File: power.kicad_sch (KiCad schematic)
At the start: 30 parts, among them J2 KYCO-P4S-S, J3 MicroFit_2x02, J3B1 DNI, J4 DC 24V/5A OUT, Q1 BC847, Q2 IRF9540SPBF, SW1 DNI, U1 MAX5035BUSA, U6 MC78M12BDTG

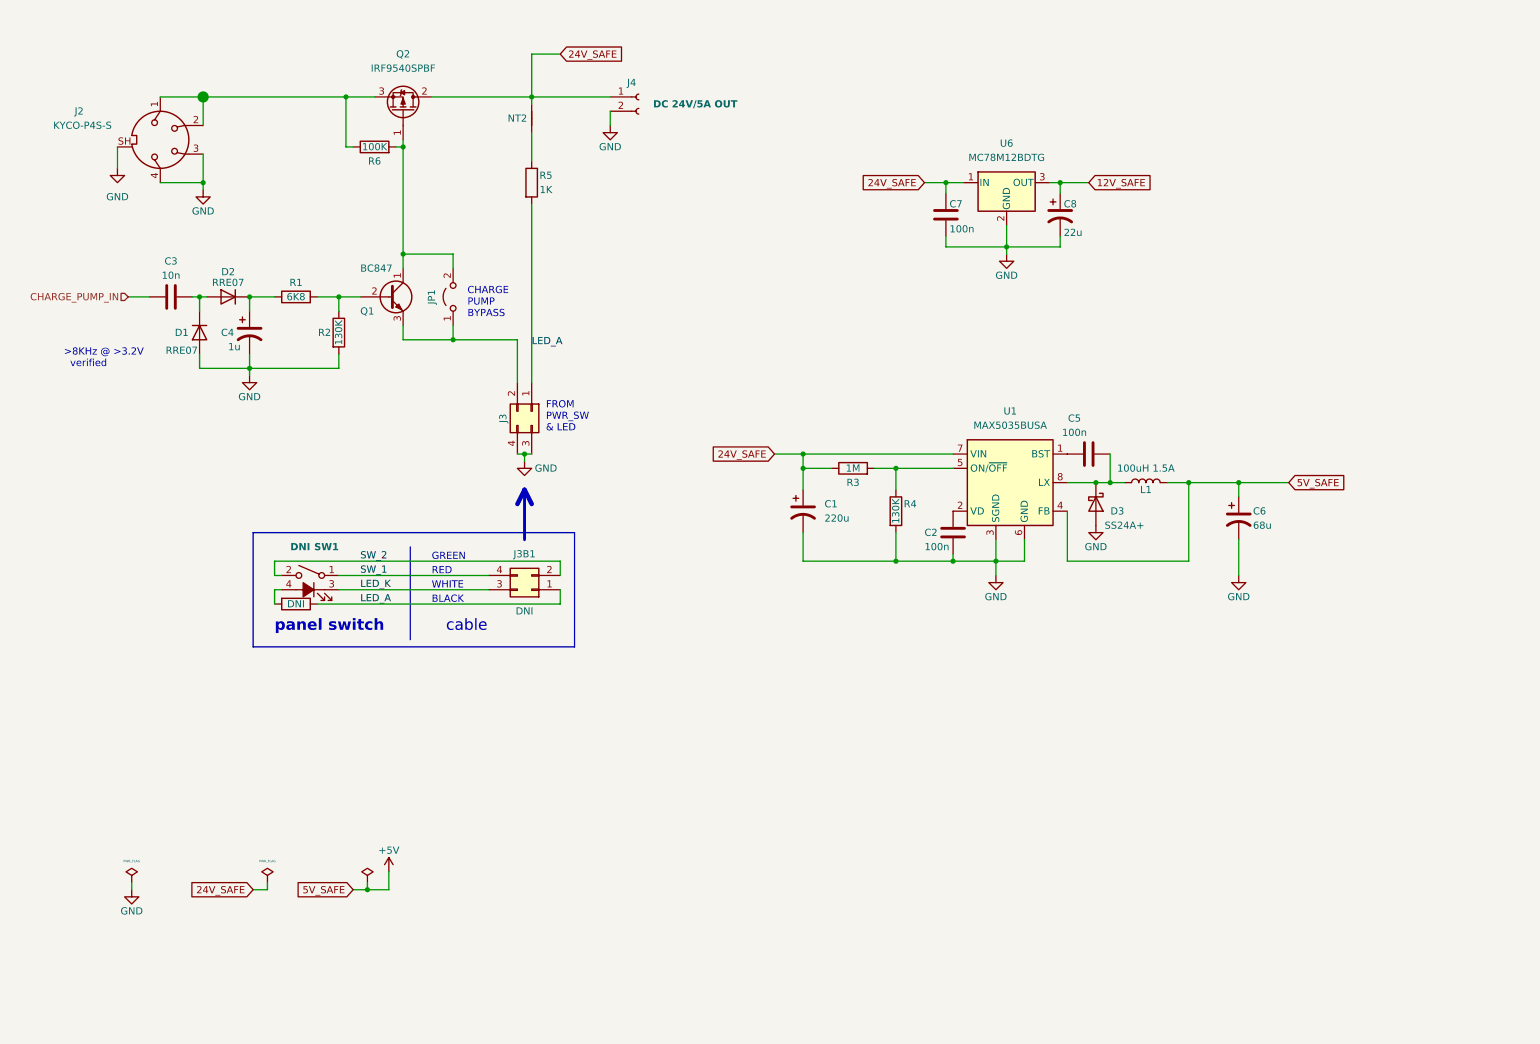
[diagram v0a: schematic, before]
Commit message: Reworked PSU control scheme (schematic only.)
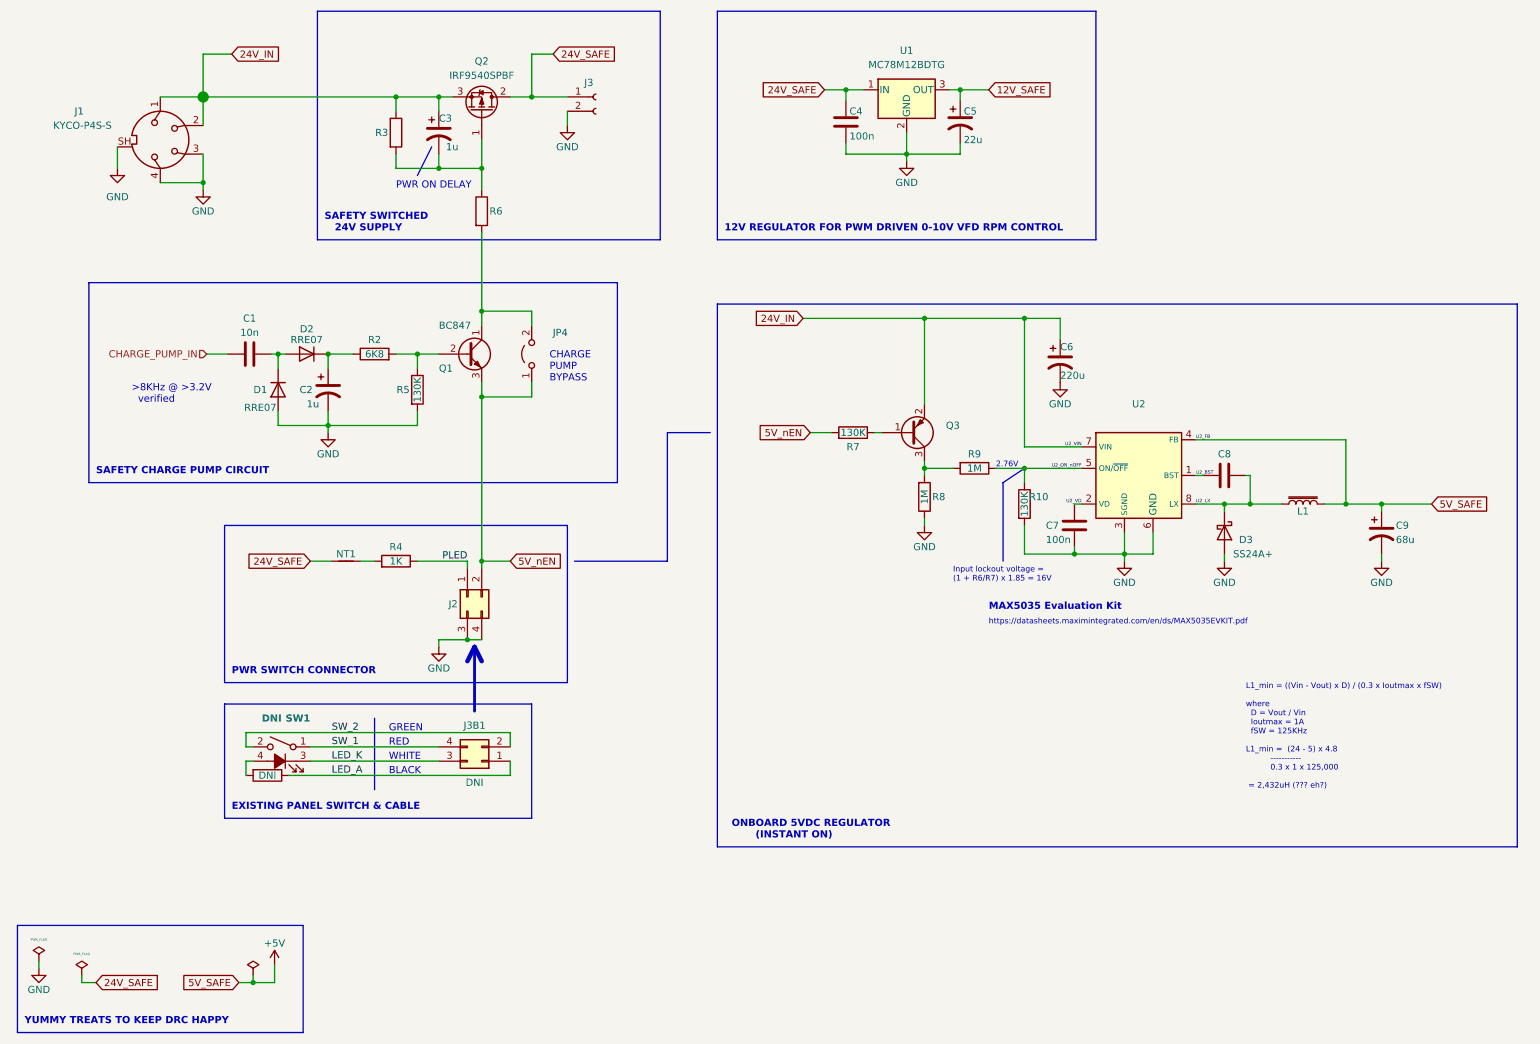
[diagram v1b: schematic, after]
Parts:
- added C3: 1u, Capacitor_SMD:C_0603_1608Metric, symbol Device:C_Polarized_US
- added Q3: (no value), Package_TO_SOT_SMD:SOT-23, symbol Transistor_BJT:BC857
- added R6: (no value), Resistor_SMD:R_0603_1608Metric, symbol Device:R
- added R7: 130K, Resistor_SMD:R_0603_1608Metric, symbol Device:R
- added R8: 1M, Resistor_SMD:R_0603_1608Metric, symbol Device:R
- C8: renamed from C5; value 100n -> (none)
- J3: renamed from J4; value DC 24V/5A OUT -> (none)
- L1: value 100uH 1.5A -> (none); footprint Inductor_SMD:L_12x12mm_H6mm -> (none); symbol Device:L -> 3rd-party:Lcore
- R3: renamed from R6; value 100K -> (none); footprint Resistor_SMD:R_0603_1608Metric -> (none)
- U2: renamed from U1; value MAX5035BUSA -> (none); footprint Package_SO:SOIC-8_3.9x4.9mm_P1.27mm -> (none); symbol Regulator_Switching:MAX5035BUSA -> 3rd-party:MAX5035BUSA
- renumbered C3 to C1, C4 to C2, C7 to C4, C8 to C5, C1 to C6, C2 to C7, C6 to C9, J2 to J1, J3 to J2, JP1 to JP4, NT2 to NT1, R101 to R1, R4 to R10, R1 to R2, R5 to R4, R2 to R5, R3 to R9, U6 to U1
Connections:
- net 24V_SAFE: no longer C6.1, R9.1, U2.7 (VIN)
- net GND: now also R8.1
- net LED_A: no longer J2.1 (Pin_1), R4.2
- net U2_LX: now reaches C8.2, D3.1 (K), L1.1, U2.8 (LX)
- net at JP4.2 (B), Q1.1 (C): now also R6.2; no longer Q2.1 (G), R3.2
- net 5V_nEN: now reaches J2.2 (Pin_2), JP4.1 (A), Q1.3 (E)
- net 5V_nEN: now also R7.2
- net U2_BST: now reaches C8.1, U2.1 (BST)
- net 24V_IN: now reaches J1.1, J1.2, Q2.3 (S), R3.1
- net 24V_IN: now also C6.1, U2.7 (VIN), C3.1, Q3.2 (E)
- net at NT1.1: now also R4.2; no longer R4.1
- net U2_ON_nOFF: now reaches R10.1, U2.5 (ON/~{OFF})
- net U2_ON_nOFF: now also R9.1; no longer R9.2
- net U2_VD: now reaches C7.1, U2.2 (VD)
- new net: Q3.1 (B), R7.1
- new net: Q3.3 (C), R8.2, R9.2
- new net: C3.2, Q2.1 (G), R3.2, R6.1
- new net PLED: J2.1 (Pin_1), R4.1
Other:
- note added: "12V REGULATOR FOR PWM DRIVEN 0-10V VFD RPM CONTROL"
- note added: "2.76V"
- note added: "EXISTING PANEL SWITCH & CABLE"
- note added: "Input lockout voltage = (1 + R6/R7) x 1.85 = 16V"
- note added: "L1_min = ((Vin - Vout) x D) / (0.3 x Ioutmax x fSW) where D = Vout / Vin Ioutmax = 1A fSW = 125KHz L1_min = (24 - 5) x 4.8 ----------- 0.3 x 1 x 125,000 = 2,432uH (??? eh?)"
- note added: "MAX5035 Evaluation Kit"
- note added: "ONBOARD 5VDC REGULATOR (INSTANT ON)"
- note added: "PWR ON DELAY"
- note added: "PWR SWITCH CONNECTOR"
- note added: "SAFETY CHARGE PUMP CIRCUIT"
- note added: "SAFETY SWITCHED 24V SUPPLY"
- note added: "YUMMY TREATS TO KEEP DRC HAPPY"
- note added: "https://datasheets.maximintegrated.com/en/ds/MAX5035EVKIT.pdf"
- note removed: "FROM PWR_SW & LED"
- note removed: "cable"
- note removed: "panel switch"
- moved on the sheet: C1, C2, C4, C5, C6, C7, C8, C9, D1, D2, D3, J2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

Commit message: sync other PC
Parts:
- C8: value (none) -> 100n/16V
- J3: value (none) -> 24V/5A OUT
- L1: value (none) -> 100uH 1.5A; footprint (none) -> Inductor_SMD:L_12x12mm_H6mm
- Q3: value (none) -> BC857
- R3: value (none) -> 1M; footprint (none) -> Resistor_SMD:R_0603_1608Metric
- R6: value (none) -> 6K8
- U2: value (none) -> MAX5035BUSA; footprint (none) -> Package_SO:SOIC-8_3.9x4.9mm_P1.27mm
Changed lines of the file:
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@@
     (stroke (width 0) (type default) (color 0 0 0 0))
   )
-  (image (at 204.47 142.24) (scale 0.30086)
+  (image (at 251.46 138.43) (scale 0.30086)
     (data
       iVBORw0KGgoAAAANSUhEUgAABWYAAAV0CAIAAADbzFNAAAAAA3NCSVQICAjb4U/gAAAACXBIWXMA
@@
     (effects (font (size 1.27 1.27)) (justify left bottom))
   )
-  (text "MAX5035 Evaluation Kit" (at 186.69 120.65 0)
+  (text "MAX5035 Evaluation Kit" (at 177.8 123.19 0)
     (effects (font (size 1.27 1.27) (thickness 0.254) bold) (justify left bottom))
   )
@@
   )
   (text "https://datasheets.maximintegrated.com/en/ds/MAX5035EVKIT.pdf"
-    (at 186.69 123.19 0)
+    (at 177.8 125.73 0)
     (effects (font (size 1 1)) (justify left bottom))
   )
@@
   )
   (text "L1_min = ((Vin - Vout) x D) / (0.3 x Ioutmax x fSW)\n\nwhere \n  D = Vout / Vin\n  Ioutmax = 1A\n  fSW = 125KHz\n\nL1_min =  (24 - 5) x 4.8\n          -----------\n          0.3 x 1 x 125,000\n\n = 2,432uH (??? eh?)"
-    (at 232.41 152.4 0)
+    (at 182.88 149.86 0)
     (effects (font (size 1 1)) (justify left bottom))
   )
@@
     (in_bom yes) (on_board yes)
     (property "Reference" "C8" (id 0) (at 228.6 92.71 90))
-    (property "Value" "" (id 1) (at 234.95 95.25 90))
+    (property "Value" "100n/16V" (id 1) (at 234.95 95.25 90))
     (property "Footprint" "Capacitor_SMD:C_0603_1608Metric" (id 2) (at 232.41 95.5548 0)
       (effects (font (size 1.27 1.27)) hide)
@@
       (effects (font (size 1.27 1.27)) (justify left))
     )
-    (property "Value" "" (id 1) (at 177.8 90.17 0)
+    (property "Value" "BC857" (id 1) (at 177.8 90.17 0)
       (effects (font (size 1.27 1.27)) (justify left))
     )
@@
     (in_bom yes) (on_board yes)
     (property "Reference" "R3" (id 0) (at 78.74 35.56 0))
-    (property "Value" "" (id 1) (at 81.28 35.56 90))
-    (property "Footprint" "" (id 2) (at 79.502 35.56 90)
+    (property "Value" "1M" (id 1) (at 81.28 35.56 90))
+    (property "Footprint" "Resistor_SMD:R_0603_1608Metric" (id 2) (at 79.502 35.56 90)
       (effects (font (size 1.27 1.27)) hide)
     )
@@
     (in_bom yes) (on_board yes)
     (property "Reference" "R6" (id 0) (at 99.06 49.53 0))
-    (property "Value" "" (id 1) (at 96.52 49.53 90))
+    (property "Value" "6K8" (id 1) (at 96.52 49.53 90))
     (property "Footprint" "Resistor_SMD:R_0603_1608Metric" (id 2) (at 94.742 49.53 90)
       (effects (font (size 1.27 1.27)) hide)
@@
     (in_bom yes) (on_board yes) (fields_autoplaced)
     (property "Reference" "U2" (id 0) (at 213.36 83.82 0))
-    (property "Value" "" (id 1) (at 213.36 86.36 0))
-    (property "Footprint" "" (id 2) (at 217.17 105.41 0)
+    (property "Value" "MAX5035BUSA" (id 1) (at 213.36 86.36 0))
+    (property "Footprint" "Package_SO:SOIC-8_3.9x4.9mm_P1.27mm" (id 2) (at 217.17 105.41 0)
       (effects (font (size 1.27 1.27) italic) (justify left) hide)
     )
@@
     (in_bom yes) (on_board yes)
     (property "Reference" "J3" (id 0) (at 115.57 26.67 0))
-    (property "Value" "" (id 1) (at 113.03 34.29 0)
+    (property "Value" "24V/5A OUT" (id 1) (at 113.03 34.29 0)
       (effects (font (size 1.27 1.27) bold) (justify left))
     )
@@
     (in_bom yes) (on_board yes)
     (property "Reference" "L1" (id 0) (at 242.57 102.87 90))
-    (property "Value" "" (id 1) (at 241.3 99.06 90))
-    (property "Footprint" "" (id 2) (at 242.57 101.6 0)
+    (property "Value" "100uH 1.5A" (id 1) (at 241.3 99.06 90))
+    (property "Footprint" "Inductor_SMD:L_12x12mm_H6mm" (id 2) (at 242.57 101.6 0)
       (effects (font (size 1.27 1.27)) hide)
     )

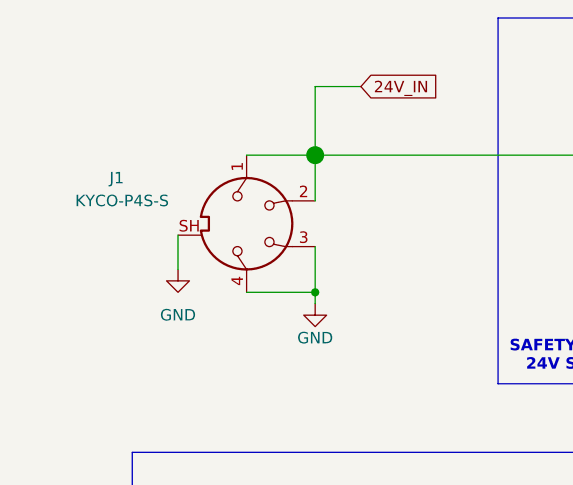
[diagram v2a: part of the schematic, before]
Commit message: Change share/_footprints to share/module with new alias '-Project'
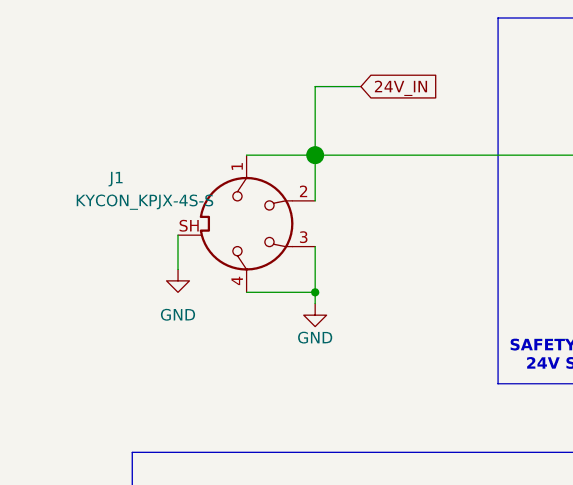
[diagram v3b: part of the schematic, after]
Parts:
- J1: value KYCO-P4S-S -> KYCON_KPJX-4S-S; footprint _footprints:KYCON_KPJX-4S-S -> -Project:KYCON_KPJX-4S-S
- NT1: footprint _footprints:NetTie-2_SMD_Pad0.3mm -> -Project:NetTie-2_SMD_Pad0.3mm
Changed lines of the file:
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@@
       (effects (font (size 1.27 1.27)) hide)
     )
-    (property "Footprint" "_footprints:NetTie-2_SMD_Pad0.3mm" (id 2) (at 72.39 111.76 0)
+    (property "Footprint" "-Project:NetTie-2_SMD_Pad0.3mm" (id 2) (at 72.39 111.76 0)
       (effects (font (size 1.27 1.27)) hide)
     )
@@
       (effects (font (size 1.27 1.27)) (justify left))
     )
-    (property "Value" "KYCO-P4S-S" (id 1) (at 20.32 34.29 90)
+    (property "Value" "KYCON_KPJX-4S-S" (id 1) (at 20.32 34.29 90)
       (effects (font (size 1.27 1.27)) (justify left))
     )
-    (property "Footprint" "_footprints:KYCON_KPJX-4S-S" (id 2) (at 39.37 36.83 0)
+    (property "Footprint" "-Project:KYCON_KPJX-4S-S" (id 2) (at 39.37 36.83 0)
       (effects (font (size 1.27 1.27)) hide)
     )

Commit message: Much to do about power
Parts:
- added NT26: NetTie_2, -Project:NetTie-2_SMD_Pad1.0mm, symbol Device:NetTie_2
- added NT27: NetTie_2, -Project:NetTie-2_SMD_Pad0.5mm, symbol Device:NetTie_2
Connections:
- net +5V: now also NT26.2; no longer C9.1, L1.2, U2.4 (FB)
- net 24V_IN: now also NT27.1; no longer Q3.2 (E), U2.7 (VIN)
- new net U2_FB: C9.1, L1.2, NT26.1, U2.4 (FB)
- new net U2_VIN: NT27.2, Q3.2 (E), U2.7 (VIN)
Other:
- moved on the sheet: C6
